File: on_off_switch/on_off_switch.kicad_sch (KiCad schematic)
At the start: 17 parts, among them K1 HFD23_005-1ZS, Q1 BC846, U1 ATtiny13A-P, U2 L78L05_SOT89

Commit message: added PCB design
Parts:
- U2: footprint Package_SO:SOIC-8_3.9x4.9mm_P1.27mm -> Package_TO_SOT_SMD:SOT-89-3_Handsoldering
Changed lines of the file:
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@@
 			)
 		)
-		(property "Footprint" "Package_SO:SOIC-8_3.9x4.9mm_P1.27mm"
+		(property "Footprint" "Package_TO_SOT_SMD:SOT-89-3_Handsoldering"
 			(at 59.69 30.48 0)
 			(effects

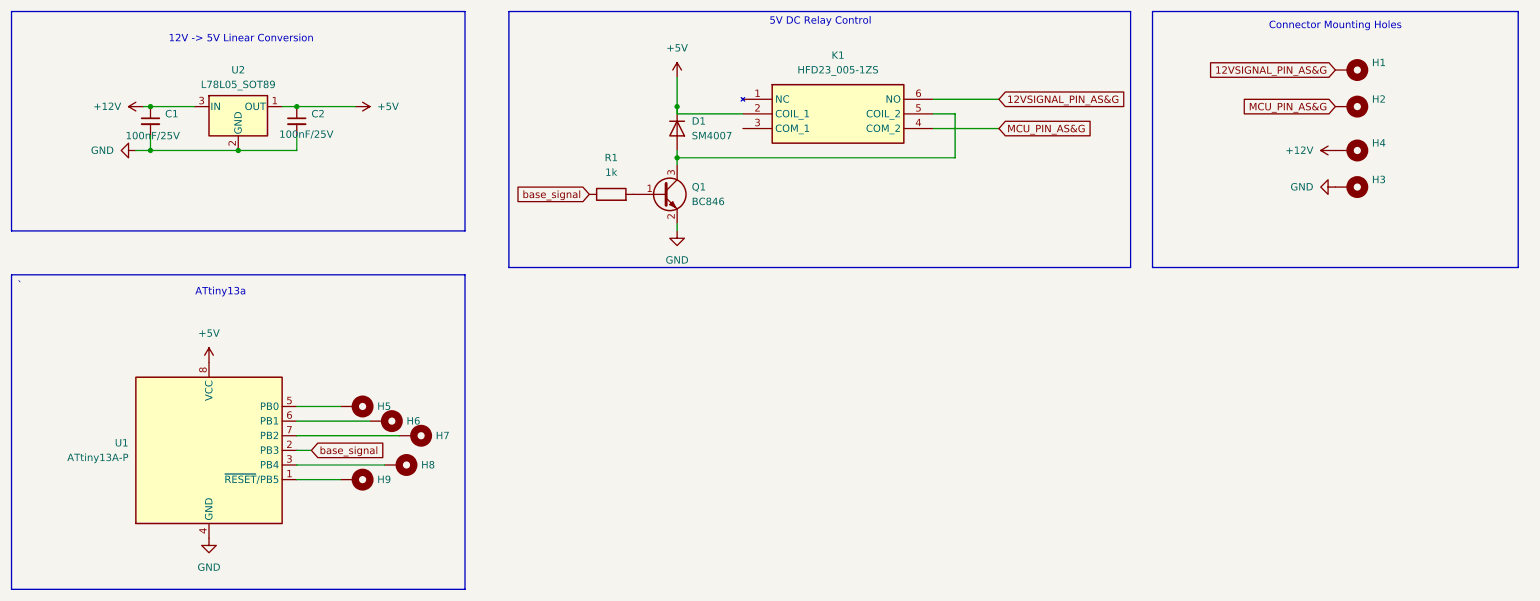
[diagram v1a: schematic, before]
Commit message: Reworked schematics and PCB
added mounting holes and renamed existing ones.
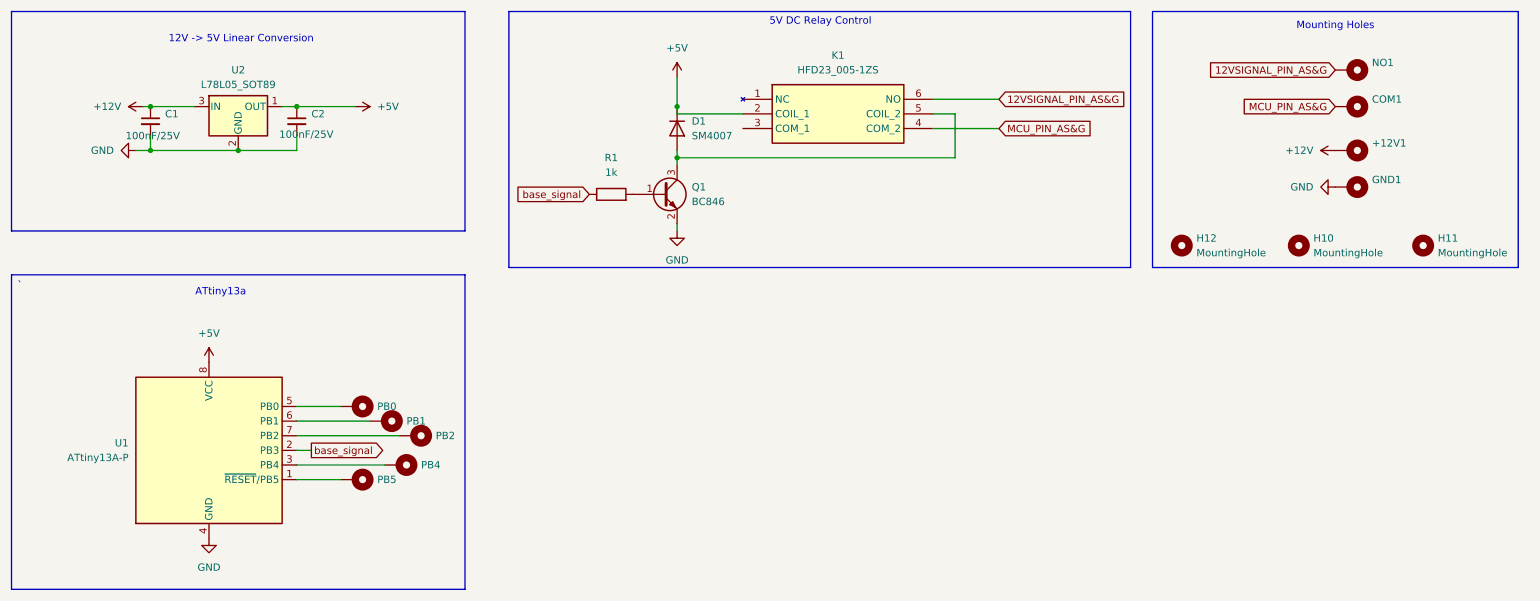
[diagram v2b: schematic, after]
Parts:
- added H10, H11, H12: MountingHole, MountingHole:MountingHole_2.1mm, symbol Mechanical:MountingHole
- renumbered H4 to +12V1, H2 to COM1, H3 to GND1, H1 to NO1, H5 to PB0, H6 to PB1, H7 to PB2, H8 to PB4, H9 to PB5
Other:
- note added: "Mounting Holes"
- note removed: "Connector Mounting Holes"
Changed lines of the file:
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@@
 		)
 	)
-	(text "Connector Mounting Holes"
+	(text "Mounting Holes"
 		(exclude_from_sim no)
 		(at 250.19 21.59 0)
@@
 	)
 	(global_label "base_signal"
-		(shape input)
+		(shape output)
 		(at 72.39 95.25 0)
 		(fields_autoplaced yes)
@@
 	)
 	(symbol
+		(lib_id "Mechanical:MountingHole")
+		(at 265.43 59.69 0)
+		(unit 1)
+		(exclude_from_sim yes)
+		(in_bom no)
+		(on_board yes)
+		(dnp no)
+		(fields_autoplaced yes)
+		(property "Reference" "H11"
+			(at 267.97 58.4199 0)
+			(effects
+				(font
+					(size 1.27 1.27)
+				)
+				(justify left)
+			)
+		)
+		(property "Value" "MountingHole"
+			(at 267.97 60.9599 0)
+			(effects
+				(font
+					(size 1.27 1.27)
+				)
+				(justify left)
+			)
+		)
+		(property "Footprint" "MountingHole:MountingHole_2.1mm"
+			(at 265.43 59.69 0)
+			(effects
+				(font
+					(size 1.27 1.27)
+				)
+				(hide yes)
+			)
+		)
+		(property "Datasheet" "~"
+			(at 265.43 59.69 0)
+			(effects
+				(font
+					(size 1.27 1.27)
+				)
+				(hide yes)
+			)
+		)
+		(property "Description" "Mounting Hole without connection"
+			(at 265.43 59.69 0)
+			(effects
+				(font
+					(size 1.27 1.27)
+				)
+				(hide yes)
+			)
+		)
+		(instances
+			(project "on_off_switch"
+				(path "/b45ad2dc-f01f-43ff-9948-db1a53e8c4bb"
+					(reference "H11")
+					(unit 1)
+				)
+			)
+		)
+	)
+	(symbol
 		(lib_id "Mechanical:MountingHole_Pad")
 		(at 80.01 100.33 270)
@@
 		(dnp no)
 		(fields_autoplaced yes)
-		(property "Reference" "H9"
+		(property "Reference" "PB5"
 			(at 83.82 100.3299 90)
 			(effects
@@
 			(project "on_off_switch"
 				(path "/b45ad2dc-f01f-43ff-9948-db1a53e8c4bb"
-					(reference "H9")
+					(reference "PB5")
 					(unit 1)
 				)
@@
 		(dnp no)
 		(fields_autoplaced yes)
-		(property "Reference" "H5"
+		(property "Reference" "PB0"
 			(at 83.82 87.6299 90)
 			(effects
@@
 			(project "on_off_switch"
 				(path "/b45ad2dc-f01f-43ff-9948-db1a53e8c4bb"
-					(reference "H5")
+					(reference "PB0")
 					(unit 1)
 				)
@@
 		(dnp no)
 		(fields_autoplaced yes)
-		(property "Reference" "H8"
+		(property "Reference" "PB4"
 			(at 91.44 97.7899 90)
 			(effects
@@
 			(project "on_off_switch"
 				(path "/b45ad2dc-f01f-43ff-9948-db1a53e8c4bb"
-					(reference "H8")
+					(reference "PB4")
 					(unit 1)
 				)
@@
 		(dnp no)
 		(fields_autoplaced yes)
-		(property "Reference" "H2"
+		(property "Reference" "COM1"
 			(at 256.54 34.2899 90)
 			(effects
@@
 			(project "on_off_switch"
 				(path "/b45ad2dc-f01f-43ff-9948-db1a53e8c4bb"
-					(reference "H2")
+					(reference "COM1")
 					(unit 1)
 				)
@@
 		(dnp no)
 		(fields_autoplaced yes)
-		(property "Reference" "H7"
+		(property "Reference" "PB2"
 			(at 93.98 92.7099 90)
 			(effects
@@
 			(project "on_off_switch"
 				(path "/b45ad2dc-f01f-43ff-9948-db1a53e8c4bb"
-					(reference "H7")
+					(reference "PB2")
 					(unit 1)
 				)
@@
 	)
 	(symbol
+		(lib_id "Mechanical:MountingHole")
+		(at 223.52 59.69 0)
+		(unit 1)
+		(exclude_from_sim yes)
+		(in_bom no)
+		(on_board yes)
+		(dnp no)
+		(fields_autoplaced yes)
+		(property "Reference" "H12"
+			(at 226.06 58.4199 0)
+			(effects
+				(font
+					(size 1.27 1.27)
+				)
+				(justify left)
+			)
+		)
+		(property "Value" "MountingHole"
+			(at 226.06 60.9599 0)
+			(effects
+				(font
+					(size 1.27 1.27)
+				)
+				(justify left)
+			)
+		)
+		(property "Footprint" "MountingHole:MountingHole_2.1mm"
+			(at 223.52 59.69 0)
+			(effects
+				(font
+					(size 1.27 1.27)
+				)
+				(hide yes)
+			)
+		)
+		(property "Datasheet" "~"
+			(at 223.52 59.69 0)
+			(effects
+				(font
+					(size 1.27 1.27)
+				)
+				(hide yes)
+			)
+		)
+		(property "Description" "Mounting Hole without connection"
+			(at 223.52 59.69 0)
+			(effects
+				(font
+					(size 1.27 1.27)
+				)
+				(hide yes)
+			)
+		)
+		(instances
+			(project "on_off_switch"
+				(path "/b45ad2dc-f01f-43ff-9948-db1a53e8c4bb"
+					(reference "H12")
+					(unit 1)
+				)
+			)
+		)
+	)
+	(symbol
 		(lib_id "power:GND")
 		(at 135.89 57.15 0)
@@
 	)
 	(symbol
+		(lib_id "Mechanical:MountingHole")
+		(at 243.84 59.69 0)
+		(unit 1)
+		(exclude_from_sim yes)
+		(in_bom no)
+		(on_board yes)
+		(dnp no)
+		(fields_autoplaced yes)
+		(property "Reference" "H10"
+			(at 246.38 58.4199 0)
+			(effects
+				(font
+					(size 1.27 1.27)
+				)
+				(justify left)
+			)
+		)
+		(property "Value" "MountingHole"
+			(at 246.38 60.9599 0)
+			(effects
+				(font
+					(size 1.27 1.27)
+				)
+				(justify left)
+			)
+		)
+		(property "Footprint" "MountingHole:MountingHole_2.1mm"
+			(at 243.84 59.69 0)
+			(effects
+				(font
+					(size 1.27 1.27)
+				)
+				(hide yes)
+			)
+		)
+		(property "Datasheet" "~"
+			(at 243.84 59.69 0)
+			(effects
+				(font
+					(size 1.27 1.27)
+				)
+				(hide yes)
+			)
+		)
+		(property "Description" "Mounting Hole without connection"
+			(at 243.84 59.69 0)
+			(effects
+				(font
+					(size 1.27 1.27)
+				)
+				(hide yes)
+			)
+		)
+		(instances
+			(project "on_off_switch"
+				(path "/b45ad2dc-f01f-43ff-9948-db1a53e8c4bb"
+					(reference "H10")
+					(unit 1)
+				)
+			)
+		)
+	)
+	(symbol
 		(lib_id "Regulator_Linear:L78L05_SOT89")
 		(at 59.69 35.56 0)
@@
 		(dnp no)
 		(fields_autoplaced yes)
-		(property "Reference" "H4"
+		(property "Reference" "+12V1"
 			(at 256.54 41.9099 90)
 			(effects
@@
 			(project "on_off_switch"
 				(path "/b45ad2dc-f01f-43ff-9948-db1a53e8c4bb"
-					(reference "H4")
+					(reference "+12V1")
 					(unit 1)
 				)
@@
 		(dnp no)
 		(fields_autoplaced yes)
-		(property "Reference" "H3"
+		(property "Reference" "GND1"
 			(at 256.54 48.2599 90)
 			(effects
@@
 			(project "on_off_switch"
 				(path "/b45ad2dc-f01f-43ff-9948-db1a53e8c4bb"
-					(reference "H3")
+					(reference "GND1")
 					(unit 1)
 				)
@@
 		(dnp no)
 		(fields_autoplaced yes)
-		(property "Reference" "H1"
+		(property "Reference" "NO1"
 			(at 256.54 27.9399 90)
 			(effects
@@
 			(project "on_off_switch"
 				(path "/b45ad2dc-f01f-43ff-9948-db1a53e8c4bb"
-					(reference "H1")
+					(reference "NO1")
 					(unit 1)
 				)
@@
 		(dnp no)
 		(fields_autoplaced yes)
-		(property "Reference" "H6"
+		(property "Reference" "PB1"
 			(at 88.9 90.1699 90)
 			(effects
@@
 			(project "on_off_switch"
 				(path "/b45ad2dc-f01f-43ff-9948-db1a53e8c4bb"
-					(reference "H6")
-					(unit 1)
-				)
+					(reference "PB1")
+					(unit 1)
+				)

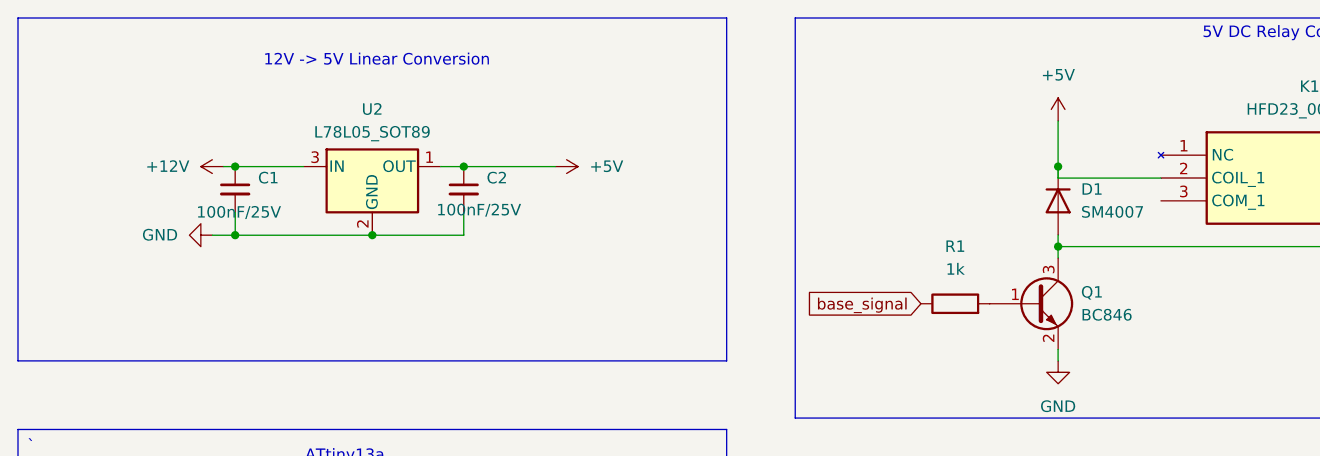
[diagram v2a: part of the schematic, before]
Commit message: Schematic and PCB change
Added reverse polarity protection diode, replaced relay diode with 1n4007, removed mounting holes
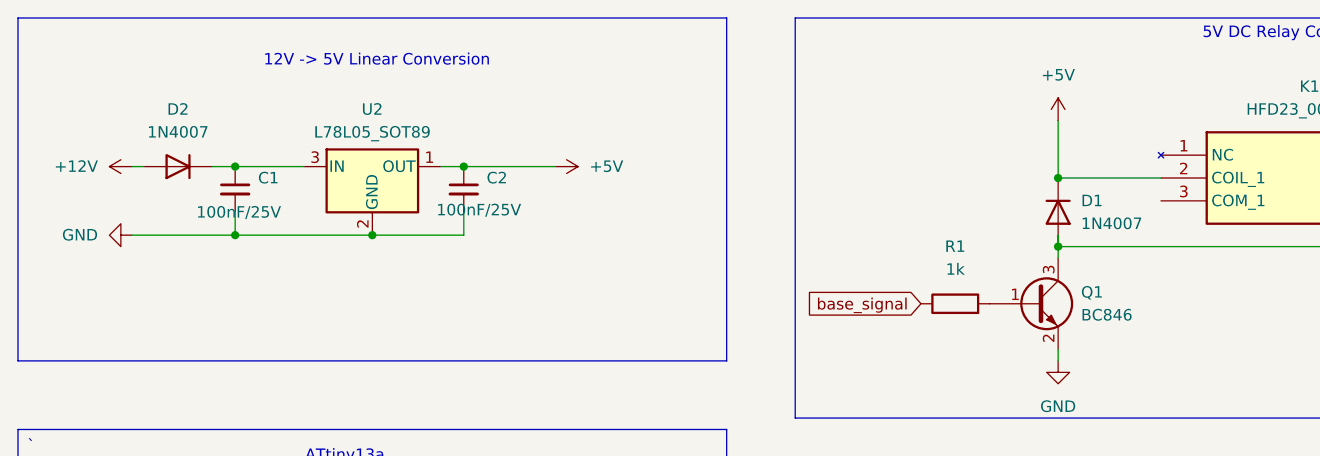
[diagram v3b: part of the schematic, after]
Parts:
- added D2: 1N4007, Diode_SMD:Nexperia_CFP3_SOD-123W, symbol Diode:SM4007
- D1: value SM4007 -> 1N4007; footprint Diode_SMD:D_MELF -> Diode_SMD:Nexperia_CFP3_SOD-123W
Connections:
- net +12V: now also D2.2 (A); no longer C1.1, U2.3 (IN)
- new net: C1.1, D2.1 (K), U2.3 (IN)
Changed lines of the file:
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@@
+	)
+	(junction
+		(at 135.89 36.83)
+		(diameter 0)
+		(color 0 0 0 0)
 	)
 	(junction
@@
 		(color 0 0 0 0)
 	)
-	(junction
-		(at 135.89 35.56)
-		(diameter 0)
-		(color 0 0 0 0)
-	)
 	(wire
 		(pts
@@
 	(wire
 		(pts
-			(xy 41.91 43.18) (xy 44.45 43.18)
+			(xy 33.02 43.18) (xy 44.45 43.18)
 		)
 		(stroke
@@
 	(wire
 		(pts
-			(xy 135.89 36.83) (xy 135.89 35.56)
+			(xy 135.89 30.48) (xy 135.89 36.83)
 		)
 		(stroke
@@
 	(wire
 		(pts
+			(xy 33.02 35.56) (xy 34.29 35.56)
+		)
+		(stroke
+			(width 0)
+			(type default)
+		)
+	)
+	(wire
+		(pts
 			(xy 44.45 40.64) (xy 44.45 43.18)
 		)
@@
 	(wire
 		(pts
+			(xy 41.91 35.56) (xy 44.45 35.56)
+		)
+		(stroke
+			(width 0)
+			(type default)
+		)
+	)
+	(wire
+		(pts
 			(xy 44.45 35.56) (xy 52.07 35.56)
 		)
@@
 	(wire
 		(pts
-			(xy 43.18 35.56) (xy 44.45 35.56)
-		)
-		(stroke
-			(width 0)
-			(type default)
-		)
-	)
-	(wire
-		(pts
 			(xy 184.15 44.45) (xy 135.89 44.45)
 		)
@@
 		(pts
 			(xy 69.85 35.56) (xy 80.01 35.56)
-		)
-		(stroke
-			(width 0)
-			(type default)
-		)
-	)
-	(wire
-		(pts
-			(xy 135.89 30.48) (xy 135.89 35.56)
 		)
 		(stroke
@@
 	)
 	(symbol
+		(lib_id "Diode:SM4007")
+		(at 38.1 35.56 180)
+		(unit 1)
+		(exclude_from_sim no)
+		(in_bom yes)
+		(on_board yes)
+		(dnp no)
+		(fields_autoplaced yes)
+		(property "Reference" "D2"
+			(at 38.1 29.21 0)
+			(effects
+				(font
+					(size 1.27 1.27)
+				)
+			)
+		)
+		(property "Value" "1N4007"
+			(at 38.1 31.75 0)
+			(effects
+				(font
+					(size 1.27 1.27)
+				)
+			)
+		)
+		(property "Footprint" "Diode_SMD:Nexperia_CFP3_SOD-123W"
+			(at 38.1 31.115 0)
+			(effects
+				(font
+					(size 1.27 1.27)
+				)
+				(hide yes)
+			)
+		)
+		(property "Datasheet" "http://cdn-reichelt.de/documents/datenblatt/A400/SMD1N400%23DIO.pdf"
+			(at 38.1 35.56 0)
+			(effects
+				(font
+					(size 1.27 1.27)
+				)
+				(hide yes)
+			)
+		)
+		(property "Description" "1000V 1A General Purpose Rectifier Diode, MELF"
+			(at 38.1 35.56 0)
+			(effects
+				(font
+					(size 1.27 1.27)
+				)
+				(hide yes)
+			)
+		)
+		(property "Sim.Device" "D"
+			(at 38.1 35.56 0)
+			(effects
+				(font
+					(size 1.27 1.27)
+				)
+				(hide yes)
+			)
+		)
+		(property "Sim.Pins" "1=K 2=A"
+			(at 38.1 35.56 0)
+			(effects
+				(font
+					(size 1.27 1.27)
+				)
+				(hide yes)
+			)
+		)
+		(pin "2"
+		)
+		(pin "1"
+		)
+		(instances
+			(project "on_off_switch"
+				(path "/b45ad2dc-f01f-43ff-9948-db1a53e8c4bb"
+					(reference "D2")
+					(unit 1)
+				)
+			)
+		)
+	)
+	(symbol
 		(lib_id "Mechanical:MountingHole")
 		(at 265.43 59.69 0)
@@
 	)
 	(symbol
+		(lib_id "Diode:SM4007")
+		(at 135.89 40.64 270)
+		(unit 1)
+		(exclude_from_sim no)
+		(in_bom yes)
+		(on_board yes)
+		(dnp no)
+		(fields_autoplaced yes)
+		(property "Reference" "D1"
+			(at 138.43 39.3699 90)
+			(effects
+				(font
+					(size 1.27 1.27)
+				)
+				(justify left)
+			)
+		)
+		(property "Value" "1N4007"
+			(at 138.43 41.9099 90)
+			(effects
+				(font
+					(size 1.27 1.27)
+				)
+				(justify left)
+			)
+		)
+		(property "Footprint" "Diode_SMD:Nexperia_CFP3_SOD-123W"
+			(at 131.445 40.64 0)
+			(effects
+				(font
+					(size 1.27 1.27)
+				)
+				(hide yes)
+			)
+		)
+		(property "Datasheet" "http://cdn-reichelt.de/documents/datenblatt/A400/SMD1N400%23DIO.pdf"
+			(at 135.89 40.64 0)
+			(effects
+				(font
+					(size 1.27 1.27)
+				)
+				(hide yes)
+			)
+		)
+		(property "Description" "1000V 1A General Purpose Rectifier Diode, MELF"
+			(at 135.89 40.64 0)
+			(effects
+				(font
+					(size 1.27 1.27)
+				)
+				(hide yes)
+			)
+		)
+		(property "Sim.Device" "D"
+			(at 135.89 40.64 0)
+			(effects
+				(font
+					(size 1.27 1.27)
+				)
+				(hide yes)
+			)
+		)
+		(property "Sim.Pins" "1=K 2=A"
+			(at 135.89 40.64 0)
+			(effects
+				(font
+					(size 1.27 1.27)
+				)
+				(hide yes)
+			)
+		)
+		(pin "2"
+		)
+		(pin "1"
+		)
+		(instances
+			(project "on_off_switch"
+				(path "/b45ad2dc-f01f-43ff-9948-db1a53e8c4bb"
+					(reference "D1")
+					(unit 1)
+				)
+			)
+		)
+	)
+	(symbol
 		(lib_id "Mechanical:MountingHole_Pad")
 		(at 80.01 100.33 270)
@@
 	(symbol
 		(lib_id "power:+12V")
-		(at 43.18 35.56 90)
+		(at 33.02 35.56 90)
 		(unit 1)
 		(exclude_from_sim no)
@@
 		(fields_autoplaced yes)
 		(property "Reference" "#PWR03"
-			(at 46.99 35.56 0)
+			(at 36.83 35.56 0)
 			(effects
 				(font
@@
 		)
 		(property "Value" "+12V"
-			(at 39.37 35.5599 90)
+			(at 29.21 35.5599 90)
 			(effects
 				(font
@@
 		)
 		(property "Footprint" ""
-			(at 43.18 35.56 0)
+			(at 33.02 35.56 0)
 			(effects
 				(font
@@
 		)
 		(property "Datasheet" ""
-			(at 43.18 35.56 0)
+			(at 33.02 35.56 0)
 			(effects
 				(font
@@
 		)
 		(property "Description" "Power symbol creates a global label with name \"+12V\""
-			(at 43.18 35.56 0)
+			(at 33.02 35.56 0)
 			(effects
 				(font
@@
 	(symbol
 		(lib_id "power:GND")
-		(at 41.91 43.18 270)
+		(at 33.02 43.18 270)
 		(unit 1)
 		(exclude_from_sim no)
@@
 		(fields_autoplaced yes)
 		(property "Reference" "#PWR05"
-			(at 35.56 43.18 0)
+			(at 26.67 43.18 0)
 			(effects
 				(font
@@
 		)
 		(property "Value" "GND"
-			(at 38.1 43.1799 90)
+			(at 29.21 43.1799 90)
 			(effects
 				(font
@@
 		)
 		(property "Footprint" ""
-			(at 41.91 43.18 0)
+			(at 33.02 43.18 0)
 			(effects
 				(font
@@
 		)
 		(property "Datasheet" ""
-			(at 41.91 43.18 0)
+			(at 33.02 43.18 0)
 			(effects
 				(font
@@
 		)
 		(property "Description" "Power symbol creates a global label with name \"GND\" , ground"
-			(at 41.91 43.18 0)
+			(at 33.02 43.18 0)
 			(effects
 				(font
@@
 					(unit 1)
 				)
-			)
-		)
-	)
-	(symbol
-		(lib_id "Diode:SM4007")
-		(at 135.89 39.37 270)
-		(unit 1)
-		(exclude_from_sim no)
-		(in_bom yes)
-		(on_board yes)
-		(dnp no)
-		(fields_autoplaced yes)
-		(property "Reference" "D1"
-			(at 138.43 38.0999 90)
-			(effects
-				(font
-					(size 1.27 1.27)
-				)
-				(justify left)
-			)
-		)
-		(property "Value" "SM4007"
-			(at 138.43 40.6399 90)
-			(effects
-				(font
-					(size 1.27 1.27)
-				)
-				(justify left)
-			)
-		)
-		(property "Footprint" "Diode_SMD:D_MELF"
-			(at 131.445 39.37 0)
-			(effects
-				(font
-					(size 1.27 1.27)
-				)
-				(hide yes)
-			)
-		)
-		(property "Datasheet" "http://cdn-reichelt.de/documents/datenblatt/A400/SMD1N400%23DIO.pdf"
-			(at 135.89 39.37 0)
-			(effects
-				(font
-					(size 1.27 1.27)
-				)
-				(hide yes)
-			)
-		)
-		(property "Description" "1000V 1A General Purpose Rectifier Diode, MELF"
-			(at 135.89 39.37 0)
-			(effects
-				(font
-					(size 1.27 1.27)
-				)
-				(hide yes)
-			)
-		)
-		(property "Sim.Device" "D"
-			(at 135.89 39.37 0)
-			(effects
-				(font
-					(size 1.27 1.27)
-				)
-				(hide yes)
-			)
-		)
-		(property "Sim.Pins" "1=K 2=A"
-			(at 135.89 39.37 0)
-			(effects
-				(font
-					(size 1.27 1.27)
-				)
-				(hide yes)
-			)
-		)
-		(pin "2"
-		)
-		(pin "1"
-		)
-		(instances
-			(project "on_off_switch"
-				(path "/b45ad2dc-f01f-43ff-9948-db1a53e8c4bb"
-					(reference "D1")
-					(unit 1)
-				)

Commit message: Added Gerbers file, modified PCB design
gerber and drill files, minor PCB changes
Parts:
- removed H10, H11, H12: MountingHole, MountingHole:MountingHole_2.1mm, symbol Mechanical:MountingHole
